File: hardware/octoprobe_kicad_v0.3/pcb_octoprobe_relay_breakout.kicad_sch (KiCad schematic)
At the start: 2 parts, among them J1001 Conn_01x20, J1002 Conn_01x20

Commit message: PCB: Octobus
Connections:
- net RELAY_OUT_6A: now reaches J1001.33 (Pin_33), J1001.34 (Pin_34), J1002.33 (Pin_33), J1002.34 (Pin_34)
- net RELAY_OUT_6B: now reaches J1001.35 (Pin_35), J1001.36 (Pin_36), J1002.35 (Pin_35), J1002.36 (Pin_36)
- net RELAY_OUT_7A: now reaches J1001.37 (Pin_37), J1001.38 (Pin_38), J1002.37 (Pin_37), J1002.38 (Pin_38)
- net RELAY_OUT_7B: now reaches J1001.39 (Pin_39), J1001.40 (Pin_40), J1002.39 (Pin_39), J1002.40 (Pin_40)
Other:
- added sheet Relay 6 (pcb_octoprobe_opto_relay.kicad_sch)
- added sheet Relay 7 (pcb_octoprobe_opto_relay.kicad_sch)
- moved on the sheet: J1001, J1002

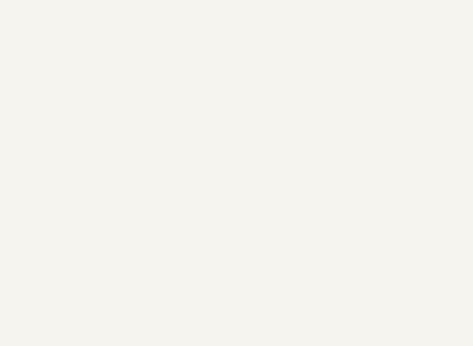
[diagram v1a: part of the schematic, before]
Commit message: PCB: Add "Open Hardware"
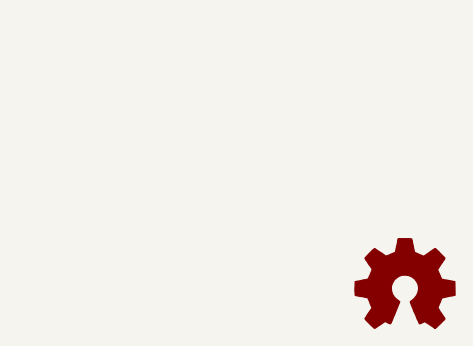
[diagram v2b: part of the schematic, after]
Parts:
- J1001, J1002: footprint 00_project_library:PinSocket_2x20_P2.54mm_Vertical-mirrored -> 00_project_library:PinSocket_2x20_P2.54mm_Vertical_squarepad
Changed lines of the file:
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@@
 			)
 		)
-		(property "Footprint" "00_project_library:PinSocket_2x20_P2.54mm_Vertical-mirrored"
+		(property "Footprint" "00_project_library:PinSocket_2x20_P2.54mm_Vertical_squarepad"
 			(at 204.47 55.88 0)
 			(effects
@@
 				(path "/35c47459-45a7-4753-acae-c8b47e7575e1/6546fe85-dd41-453d-98b0-9b6f35fb87fd"
 					(reference "J1002")
+					(unit 1)
+				)
+			)
+		)
+	)
+	(symbol
+		(lib_id "Graphic:Logo_Open_Hardware_Small")
+		(at 274.32 173.99 0)
+		(unit 1)
+		(exclude_from_sim yes)
+		(in_bom no)
+		(on_board no)
+		(dnp no)
+		(fields_autoplaced yes)
+		(property "Reference" "#SYM501"
+			(at 274.32 167.005 0)
+			(effects
+				(font
+					(size 1.27 1.27)
+				)
+				(hide yes)
+			)
+		)
+		(property "Value" "Logo_Open_Hardware_Small"
+			(at 274.32 179.705 0)
+			(effects
+				(font
+					(size 1.27 1.27)
+				)
+				(hide yes)
+			)
+		)
+		(property "Footprint" ""
+			(at 274.32 173.99 0)
+			(effects
+				(font
+					(size 1.27 1.27)
+				)
+				(hide yes)
+			)
+		)
+		(property "Datasheet" "~"
+			(at 274.32 173.99 0)
+			(effects
+				(font
+					(size 1.27 1.27)
+				)
+				(hide yes)
+			)
+		)
+		(property "Description" "Open Hardware logo, small"
+			(at 274.32 173.99 0)
+			(effects
+				(font
+					(size 1.27 1.27)
+				)
+				(hide yes)
+			)
+		)
+		(instances
+			(project "pcb_octoprobe"
+				(path "/35c47459-45a7-4753-acae-c8b47e7575e1/6546fe85-dd41-453d-98b0-9b6f35fb87fd"
+					(reference "#SYM501")
 					(unit 1)
 				)
@@
 			)
 		)
-		(property "Footprint" "00_project_library:PinSocket_2x20_P2.54mm_Vertical-mirrored"
+		(property "Footprint" "00_project_library:PinSocket_2x20_P2.54mm_Vertical_squarepad"
 			(at 189.23 55.88 0)
 			(effects

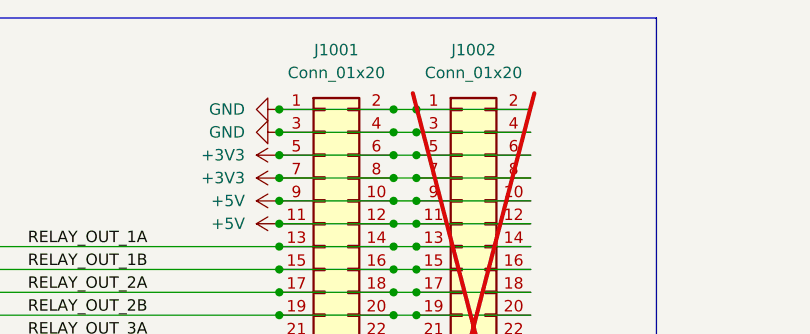
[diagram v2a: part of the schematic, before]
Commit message: PCB: Production files ready
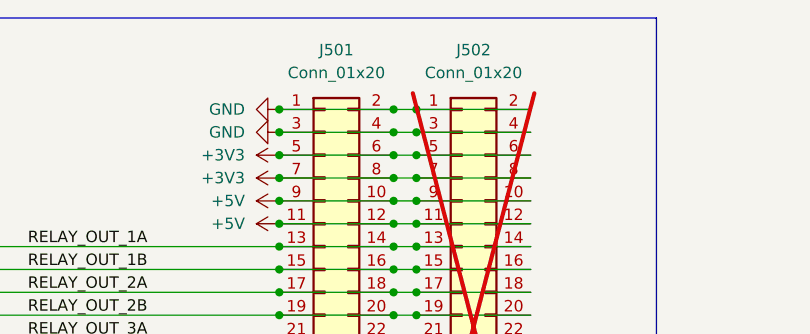
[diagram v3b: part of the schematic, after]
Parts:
- renumbered J1001 to J501, J1002 to J502
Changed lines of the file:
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@@
 	(title_block
 		(title "Octoprobe tentacle")
-		(date "2024-07-31")
+		(date "2024-08-04")
 		(rev "0.3")
 		(company "Hans Märki, Märki Informatik")
@@
 		(on_board yes)
 		(dnp no)
-		(property "Reference" "#PWR01003"
+		(property "Reference" "#PWR0503"
 			(at 187.96 38.1 0)
 			(effects
@@
 			(project "pcb_octoprobe"
 				(path "/35c47459-45a7-4753-acae-c8b47e7575e1/6546fe85-dd41-453d-98b0-9b6f35fb87fd"
-					(reference "#PWR01003")
+					(reference "#PWR0503")
 					(unit 1)
 				)
@@
 		(dnp yes)
 		(fields_autoplaced yes)
-		(property "Reference" "J1002"
+		(property "Reference" "J502"
 			(at 205.74 26.416 0)
 			(effects
@@
 			(project "pcb_octoprobe"
 				(path "/35c47459-45a7-4753-acae-c8b47e7575e1/6546fe85-dd41-453d-98b0-9b6f35fb87fd"
-					(reference "J1002")
+					(reference "J502")
 					(unit 1)
 				)
@@
 		(on_board yes)
 		(dnp no)
-		(property "Reference" "#PWR01004"
+		(property "Reference" "#PWR0504"
 			(at 187.96 40.64 0)
 			(effects
@@
 			(project "pcb_octoprobe"
 				(path "/35c47459-45a7-4753-acae-c8b47e7575e1/6546fe85-dd41-453d-98b0-9b6f35fb87fd"
-					(reference "#PWR01004")
+					(reference "#PWR0504")
 					(unit 1)
 				)
@@
 		(dnp no)
 		(fields_autoplaced yes)
-		(property "Reference" "#PWR01001"
+		(property "Reference" "#PWR0501"
 			(at 177.8 33.02 0)
 			(effects
@@
 			(project "pcb_octoprobe"
 				(path "/35c47459-45a7-4753-acae-c8b47e7575e1/6546fe85-dd41-453d-98b0-9b6f35fb87fd"
-					(reference "#PWR01001")
+					(reference "#PWR0501")
 					(unit 1)
 				)
@@
 		(dnp no)
 		(fields_autoplaced yes)
-		(property "Reference" "J1001"
+		(property "Reference" "J501"
 			(at 190.5 26.416 0)
 			(effects
@@
 			(project "pcb_octoprobe"
 				(path "/35c47459-45a7-4753-acae-c8b47e7575e1/6546fe85-dd41-453d-98b0-9b6f35fb87fd"
-					(reference "J1001")
+					(reference "J501")
 					(unit 1)
 				)
@@
 		(on_board yes)
 		(dnp no)
-		(property "Reference" "#PWR01006"
+		(property "Reference" "#PWR0506"
 			(at 187.96 45.72 0)
 			(effects
@@
 			(project "pcb_octoprobe"
 				(path "/35c47459-45a7-4753-acae-c8b47e7575e1/6546fe85-dd41-453d-98b0-9b6f35fb87fd"
-					(reference "#PWR01006")
+					(reference "#PWR0506")
 					(unit 1)
 				)
@@
 		(dnp no)
 		(fields_autoplaced yes)
-		(property "Reference" "#PWR01002"
+		(property "Reference" "#PWR0502"
 			(at 177.8 35.56 0)
 			(effects
@@
 			(project "pcb_octoprobe"
 				(path "/35c47459-45a7-4753-acae-c8b47e7575e1/6546fe85-dd41-453d-98b0-9b6f35fb87fd"
-					(reference "#PWR01002")
+					(reference "#PWR0502")
 					(unit 1)
 				)
@@
 		(on_board yes)
 		(dnp no)
-		(property "Reference" "#PWR01005"
+		(property "Reference" "#PWR0505"
 			(at 187.96 43.18 0)
 			(effects
@@
 			(project "pcb_octoprobe"
 				(path "/35c47459-45a7-4753-acae-c8b47e7575e1/6546fe85-dd41-453d-98b0-9b6f35fb87fd"
-					(reference "#PWR01005")
+					(reference "#PWR0505")
 					(unit 1)
 				)
